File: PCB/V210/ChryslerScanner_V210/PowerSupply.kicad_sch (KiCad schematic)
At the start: 32 parts, among them J4 PROG EN, U5 SDB628, U6 TD1509, U7 TD1509P5, U8 AMS1117-3.3, U9 LM317_SOT-223

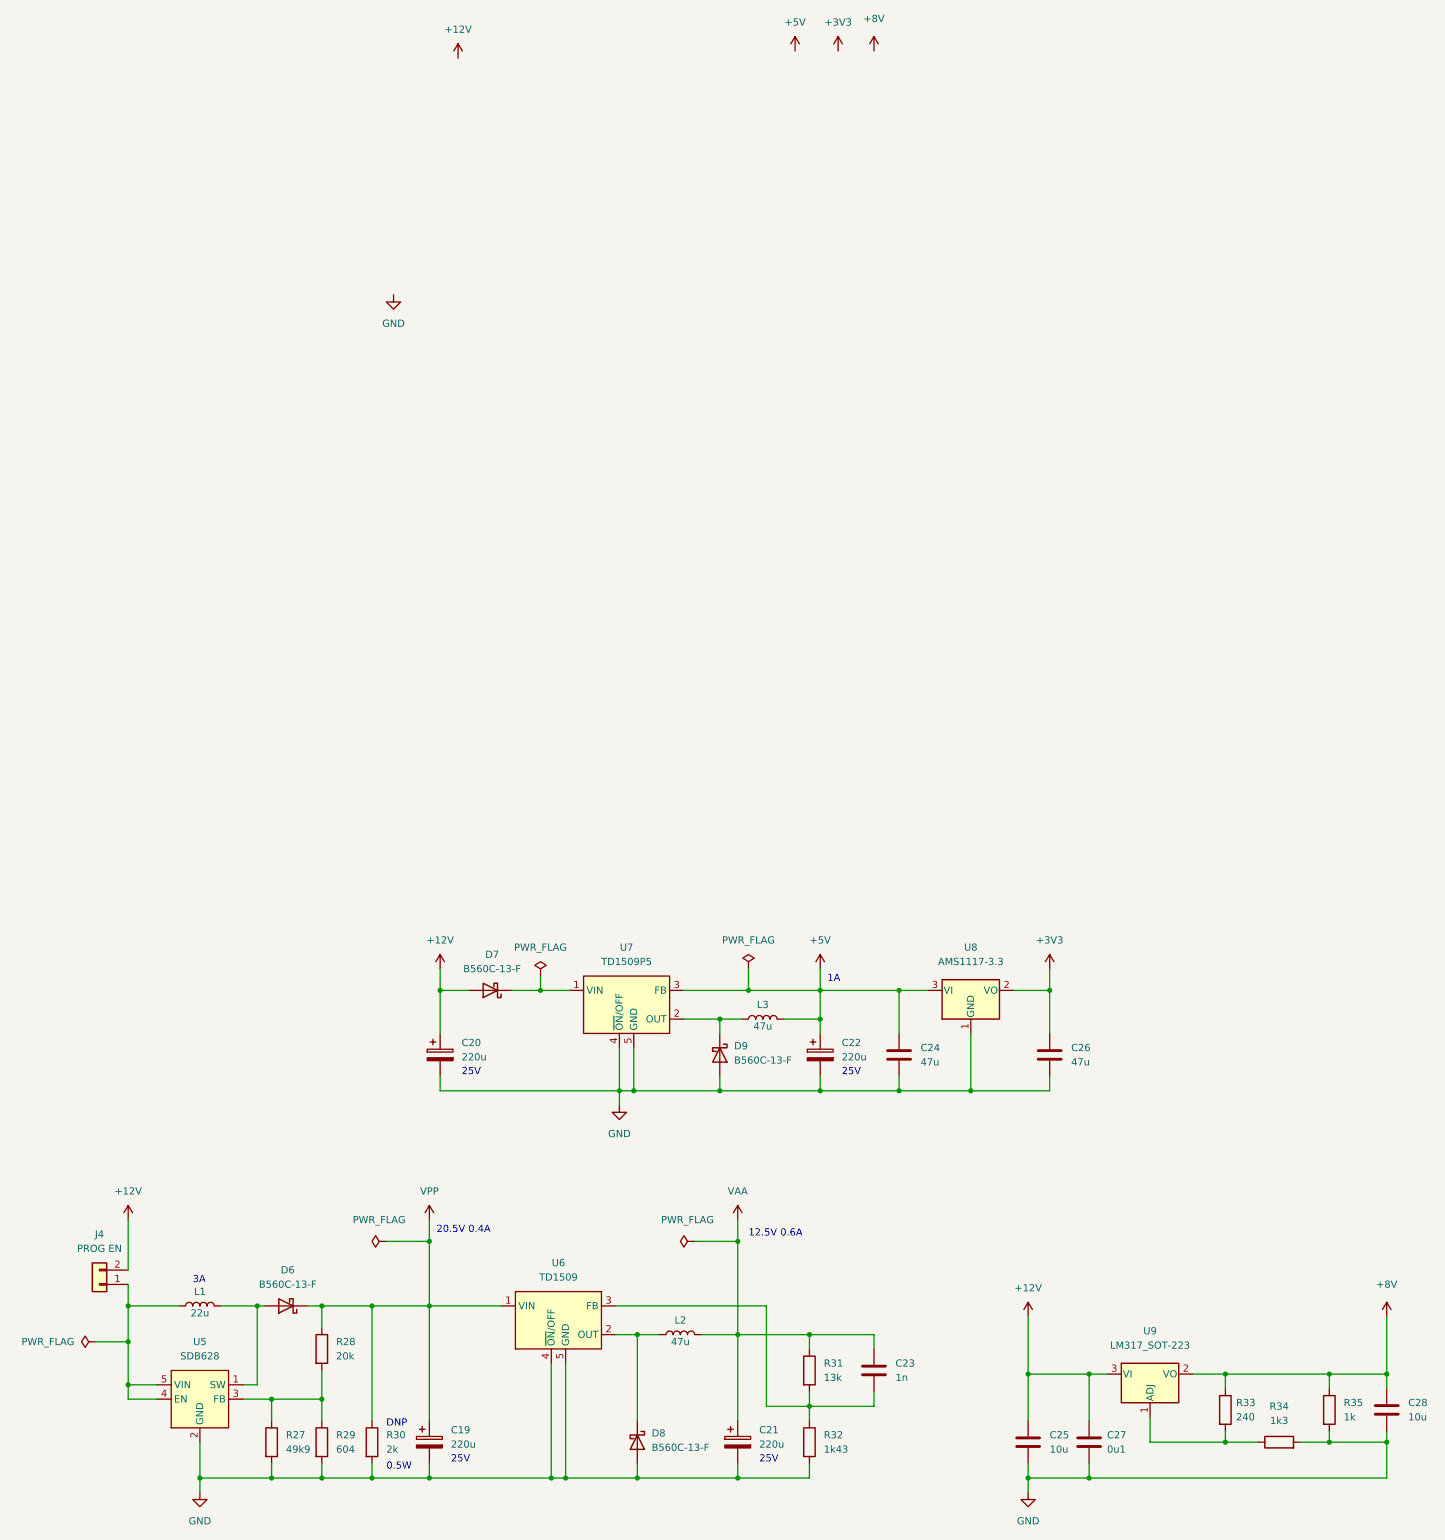
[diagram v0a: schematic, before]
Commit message: Working on power supplies. Added datasheets.
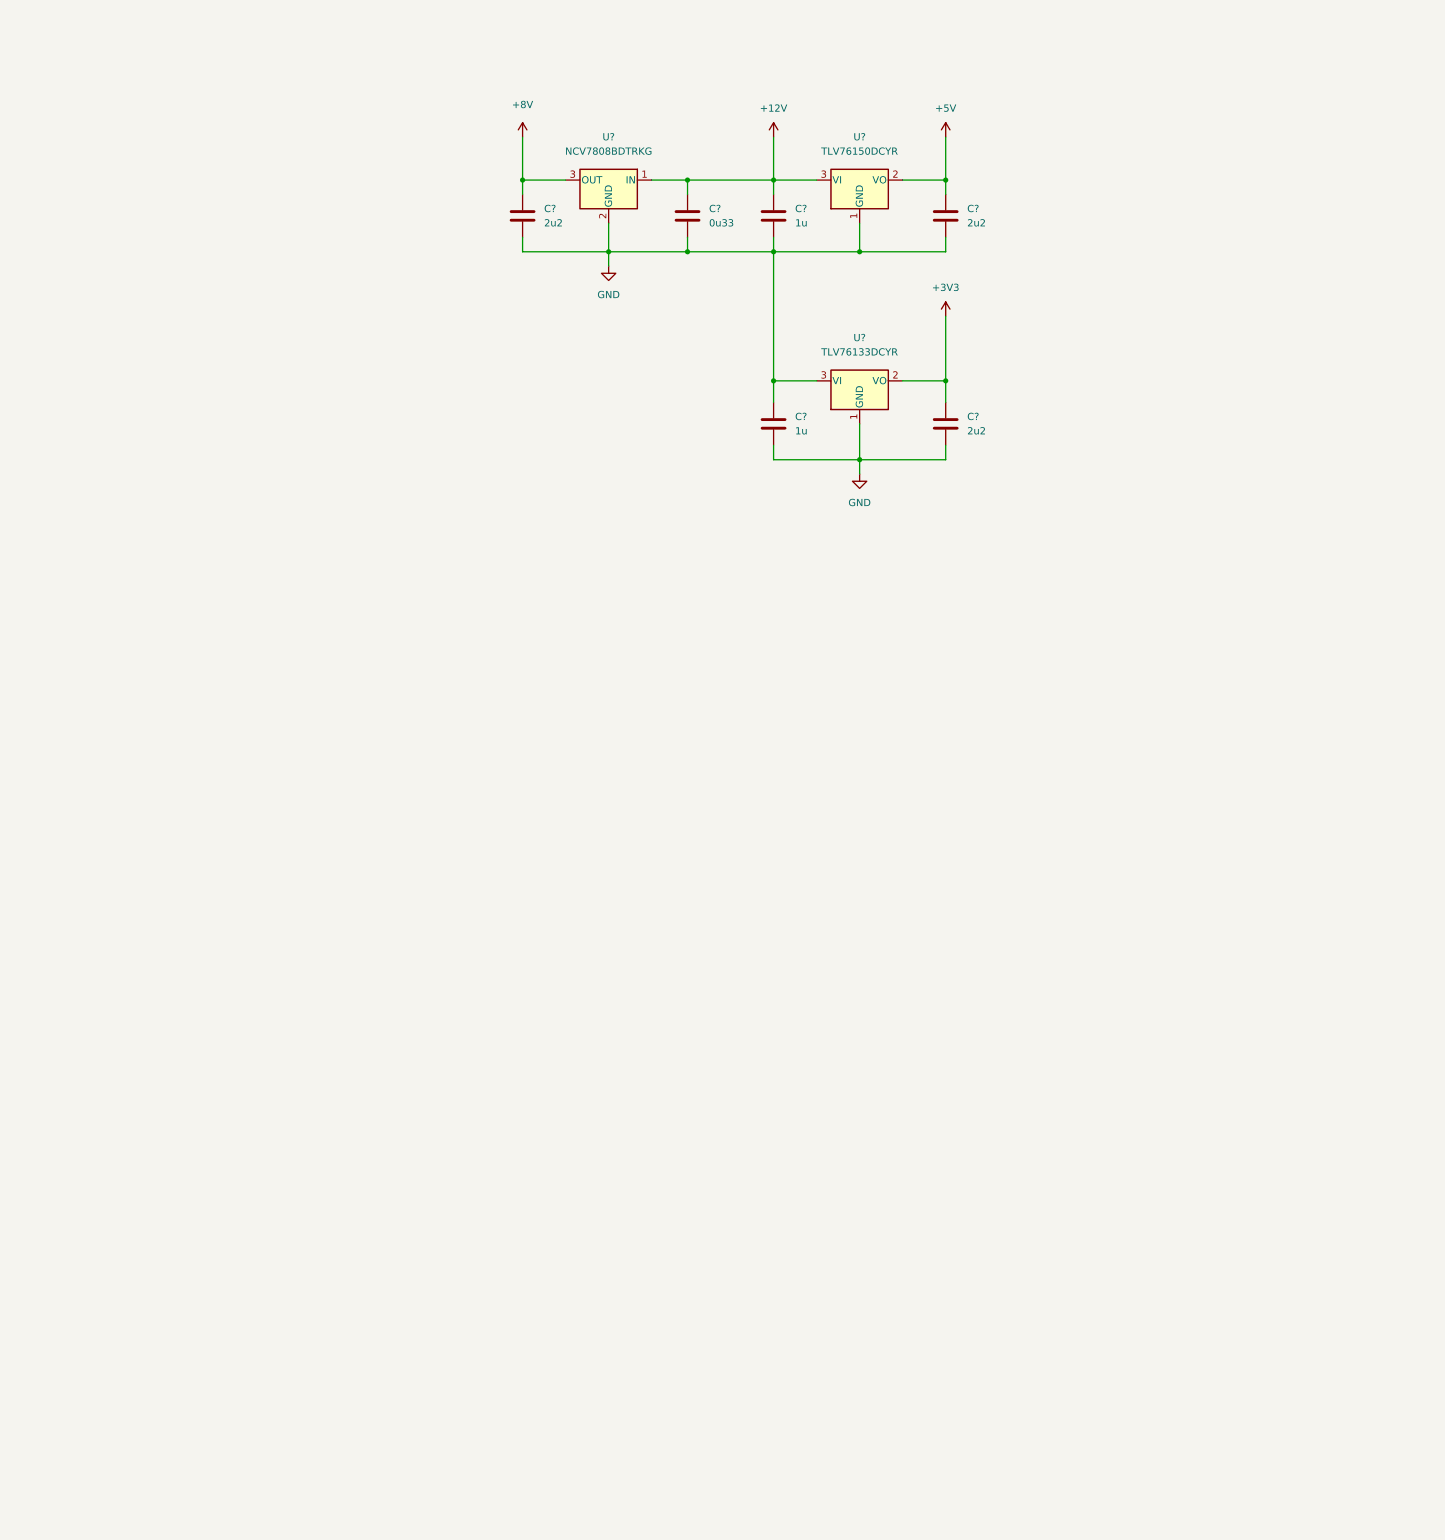
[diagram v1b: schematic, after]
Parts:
- removed C19, C20, C21, C22: 220u, symbol Device:C_Polarized
- removed C23: 1n, Capacitor_SMD:C_0603_1608Metric, symbol Device:C
- removed C24, C26: 47u, symbol Device:C
- removed C25, C28: 10u, Capacitor_SMD:C_0603_1608Metric, symbol Device:C
- removed C27: 0u1, Capacitor_SMD:C_0603_1608Metric, symbol Device:C
- removed D6, D7, D8, D9: B560C-13-F, Diode_SMD:D_SMC, symbol Device:D_Schottky
- removed J4: PROG EN, Connector_PinHeader_2.54mm:PinHeader_1x02_P2.54mm_Vertical, symbol Connector_Generic:Conn_01x02
- removed L1: 22u, symbol Device:L
- removed L2, L3: 47u, symbol Device:L
- removed R27: 49k9, Resistor_SMD:R_0603_1608Metric, symbol Device:R
- removed R28: 20k, Resistor_SMD:R_0603_1608Metric, symbol Device:R
- removed R29: 604, Resistor_SMD:R_0603_1608Metric, symbol Device:R
- removed R30: 2k, Resistor_SMD:R_0603_1608Metric, symbol Device:R
- removed R31: 13k, Resistor_SMD:R_0603_1608Metric, symbol Device:R
- removed R32: 1k43, Resistor_SMD:R_0603_1608Metric, symbol Device:R
- removed R33: 240, Resistor_SMD:R_0603_1608Metric, symbol Device:R
- removed R34: 1k3, Resistor_SMD:R_0603_1608Metric, symbol Device:R
- removed R35: 1k, Resistor_SMD:R_0603_1608Metric, symbol Device:R
- removed U5: SDB628, symbol ChryslerScanner:SD8628
- removed U6: TD1509, symbol ChryslerScanner:TD1509
- removed U7: TD1509P5, symbol ChryslerScanner:TD1509
- removed U8: AMS1117-3.3, symbol Regulator_Linear:AMS1117-3.3
- removed U9: LM317_SOT-223, symbol Regulator_Linear:LM317_SOT-223
- added C?: 0u33, symbol Device:C
- added C? (x3): 2u2, symbol Device:C
- added C? (x2): 1u, symbol Device:C
- added U?: NCV7808BDTRKG, Package_TO_SOT_SMD:TO-252-2, symbol ChryslerScanner:NCV7808BDTRKG
- added U?: TLV76133DCYR, Package_TO_SOT_SMD:SOT-223-3_TabPin2, symbol Regulator_Linear:LM1117-3.3
- added U?: TLV76150DCYR, Package_TO_SOT_SMD:SOT-223-3_TabPin2, symbol Regulator_Linear:LM1117-5.0
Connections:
- net +12V: now also C?.1, C?.1, U?.1 (IN), U?.3 (VI)
- net +3V3: now also C?.1, U?.2 (VO)
- net +5V: now also C?.1, U?.2 (VO)
- net +8V: now also C?.1, U?.3 (OUT)
- net GND: now also C?.1, C?.2, C?.2, C?.2, C?.2, C?.2, C?.2, U?.1 (GND), U?.1 (GND), U?.2 (GND), U?.3 (VI)
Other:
- note removed: "0.5W"
- note removed: "12.5V 0.6A"
- note removed: "1A"
- note removed: "20.5V 0.4A"
- note removed: "25V"
- note removed: "3A"
- note removed: "DNP"

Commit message: Added OBD-II connector.
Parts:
- gave numbers to parts that had none: 9
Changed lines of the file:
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@@
   (title_block
     (title "TJ Diag")
-    (date "2023-07-01")
+    (date "2023-07-06")
     (rev "V1.00")
     (company "andy@britishideas.com")
     (comment 1 "V210/ChryslerScanner_V210/schematic/ChryslerScanner_V210_schematic.pdf")
-    (comment 2 "Developed From: https://github.com/laszlodaniel/ChryslerScanner/blob/master/PCB/")
+    (comment 2 "Based on: https://github.com/laszlodaniel/ChryslerScanner/blob/master/PCB/")
     (comment 3 "GPL V3 LICENSE")
   )
@@
   (symbol (lib_id "Device:C") (at 137.16 85.09 0) (unit 1)
     (in_bom yes) (on_board yes) (fields_autoplaced)
-    (property "Reference" "C?" (id 0) (at 140.97 83.8199 0)
+    (property "Reference" "C20" (id 0) (at 140.97 83.8199 0)
       (effects (font (size 1.27 1.27)) (justify left))
     )
@@
   (symbol (lib_id "power:+3V3") (at 182.88 102.87 0) (unit 1)
     (in_bom yes) (on_board yes) (fields_autoplaced)
-    (property "Reference" "#PWR051" (id 0) (at 182.88 106.68 0)
+    (property "Reference" "#PWR046" (id 0) (at 182.88 106.68 0)
       (effects (font (size 1.27 1.27)) hide)
     )
@@
   (symbol (lib_id "ChryslerScanner:NCV7808BDTRKG") (at 123.19 78.74 0) (mirror y) (unit 1)
     (in_bom yes) (on_board yes) (fields_autoplaced)
-    (property "Reference" "U?" (id 0) (at 123.19 71.12 0))
+    (property "Reference" "U5" (id 0) (at 123.19 71.12 0))
     (property "Value" "NCV7808BDTRKG" (id 1) (at 123.19 73.66 0))
     (property "Footprint" "Package_TO_SOT_SMD:TO-252-2" (id 2) (at 123.19 73.66 0)
@@
   (symbol (lib_id "Device:C") (at 182.88 121.92 0) (unit 1)
     (in_bom yes) (on_board yes) (fields_autoplaced)
-    (property "Reference" "C?" (id 0) (at 186.69 120.6499 0)
+    (property "Reference" "C24" (id 0) (at 186.69 120.6499 0)
       (effects (font (size 1.27 1.27)) (justify left))
     )
@@
   (symbol (lib_id "Device:C") (at 107.95 85.09 0) (unit 1)
     (in_bom yes) (on_board yes) (fields_autoplaced)
-    (property "Reference" "C?" (id 0) (at 111.76 83.8199 0)
+    (property "Reference" "C19" (id 0) (at 111.76 83.8199 0)
       (effects (font (size 1.27 1.27)) (justify left))
     )
@@
   (symbol (lib_id "power:GND") (at 123.19 93.98 0) (unit 1)
     (in_bom yes) (on_board yes) (fields_autoplaced)
-    (property "Reference" "#PWR043" (id 0) (at 123.19 100.33 0)
+    (property "Reference" "#PWR042" (id 0) (at 123.19 100.33 0)
       (effects (font (size 1.27 1.27)) hide)
     )
@@
   (symbol (lib_id "power:+5V") (at 182.88 71.12 0) (unit 1)
     (in_bom yes) (on_board yes) (fields_autoplaced)
-    (property "Reference" "#PWR049" (id 0) (at 182.88 74.93 0)
+    (property "Reference" "#PWR045" (id 0) (at 182.88 74.93 0)
       (effects (font (size 1.27 1.27)) hide)
     )
@@
   (symbol (lib_id "Regulator_Linear:LM1117-3.3") (at 167.64 114.3 0) (unit 1)
     (in_bom yes) (on_board yes) (fields_autoplaced)
-    (property "Reference" "U?" (id 0) (at 167.64 106.68 0))
+    (property "Reference" "U7" (id 0) (at 167.64 106.68 0))
     (property "Value" "TLV76133DCYR" (id 1) (at 167.64 109.22 0))
     (property "Footprint" "Package_TO_SOT_SMD:SOT-223-3_TabPin2" (id 2) (at 167.64 114.3 0)
@@
   (symbol (lib_id "power:GND") (at 167.64 130.81 0) (unit 1)
     (in_bom yes) (on_board yes) (fields_autoplaced)
-    (property "Reference" "#PWR?" (id 0) (at 167.64 137.16 0)
+    (property "Reference" "#PWR044" (id 0) (at 167.64 137.16 0)
       (effects (font (size 1.27 1.27)) hide)
     )
@@
   (symbol (lib_id "Device:C") (at 182.88 85.09 0) (unit 1)
     (in_bom yes) (on_board yes) (fields_autoplaced)
-    (property "Reference" "C?" (id 0) (at 186.69 83.8199 0)
+    (property "Reference" "C23" (id 0) (at 186.69 83.8199 0)
       (effects (font (size 1.27 1.27)) (justify left))
     )
@@
   (symbol (lib_id "power:+8V") (at 107.95 71.12 0) (unit 1)
     (in_bom yes) (on_board yes) (fields_autoplaced)
-    (property "Reference" "#PWR052" (id 0) (at 107.95 74.93 0)
+    (property "Reference" "#PWR041" (id 0) (at 107.95 74.93 0)
       (effects (font (size 1.27 1.27)) hide)
     )
@@
   (symbol (lib_id "Device:C") (at 152.4 121.92 0) (unit 1)
     (in_bom yes) (on_board yes) (fields_autoplaced)
-    (property "Reference" "C?" (id 0) (at 156.21 120.6499 0)
+    (property "Reference" "C22" (id 0) (at 156.21 120.6499 0)
       (effects (font (size 1.27 1.27)) (justify left))
     )
@@
   (symbol (lib_id "Regulator_Linear:LM1117-5.0") (at 167.64 78.74 0) (unit 1)
     (in_bom yes) (on_board yes) (fields_autoplaced)
-    (property "Reference" "U?" (id 0) (at 167.64 71.12 0))
+    (property "Reference" "U6" (id 0) (at 167.64 71.12 0))
     (property "Value" "TLV76150DCYR" (id 1) (at 167.64 73.66 0))
     (property "Footprint" "Package_TO_SOT_SMD:SOT-223-3_TabPin2" (id 2) (at 167.64 78.74 0)
@@
   (symbol (lib_id "Device:C") (at 152.4 85.09 0) (unit 1)
     (in_bom yes) (on_board yes) (fields_autoplaced)
-    (property "Reference" "C?" (id 0) (at 156.21 83.8199 0)
+    (property "Reference" "C21" (id 0) (at 156.21 83.8199 0)
       (effects (font (size 1.27 1.27)) (justify left))
     )
@@
   (symbol (lib_id "power:+12V") (at 152.4 71.12 0) (unit 1)
     (in_bom yes) (on_board yes) (fields_autoplaced)
-    (property "Reference" "#PWR046" (id 0) (at 152.4 74.93 0)
-      (effects (font (size 1.27 1.27)) hide)
-    )
+    (property "Reference" "#PWR043" (id 0) (at 152.4 74.93 0)
+      (effects (font (size 1.27 1.27)) hide)
+    )

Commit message: Added CCD back in - needed for early TJs.
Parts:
- C17: renamed from C19; footprint (none) -> Capacitor_SMD:C_0603_1608Metric
- C18: renamed from C20; footprint (none) -> Capacitor_SMD:C_0603_1608Metric
- C19: renamed from C21; footprint (none) -> Capacitor_SMD:C_0603_1608Metric
- C20: renamed from C22; footprint (none) -> Capacitor_SMD:C_0603_1608Metric
- C21: renamed from C23; footprint (none) -> Capacitor_SMD:C_0603_1608Metric
- C22: renamed from C24; footprint (none) -> Capacitor_SMD:C_0603_1608Metric
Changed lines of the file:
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@@
   (title_block
     (title "TJ Diag")
-    (date "2023-07-06")
+    (date "2023-07-07")
     (rev "V1.00")
     (company "andy@britishideas.com")
@@
   (symbol (lib_id "Device:C") (at 137.16 85.09 0) (unit 1)
     (in_bom yes) (on_board yes) (fields_autoplaced)
-    (property "Reference" "C20" (id 0) (at 140.97 83.8199 0)
+    (property "Reference" "C18" (id 0) (at 140.97 83.8199 0)
       (effects (font (size 1.27 1.27)) (justify left))
     )
@@
       (effects (font (size 1.27 1.27)) (justify left))
     )
-    (property "Footprint" "" (id 2) (at 138.1252 88.9 0)
+    (property "Footprint" "Capacitor_SMD:C_0603_1608Metric" (id 2) (at 138.1252 88.9 0)
       (effects (font (size 1.27 1.27)) hide)
     )
@@
   (symbol (lib_id "power:+3V3") (at 182.88 102.87 0) (unit 1)
     (in_bom yes) (on_board yes) (fields_autoplaced)
-    (property "Reference" "#PWR046" (id 0) (at 182.88 106.68 0)
+    (property "Reference" "#PWR042" (id 0) (at 182.88 106.68 0)
       (effects (font (size 1.27 1.27)) hide)
     )
@@
   (symbol (lib_id "Device:C") (at 182.88 121.92 0) (unit 1)
     (in_bom yes) (on_board yes) (fields_autoplaced)
-    (property "Reference" "C24" (id 0) (at 186.69 120.6499 0)
+    (property "Reference" "C22" (id 0) (at 186.69 120.6499 0)
       (effects (font (size 1.27 1.27)) (justify left))
     )
@@
       (effects (font (size 1.27 1.27)) (justify left))
     )
-    (property "Footprint" "" (id 2) (at 183.8452 125.73 0)
+    (property "Footprint" "Capacitor_SMD:C_0603_1608Metric" (id 2) (at 183.8452 125.73 0)
       (effects (font (size 1.27 1.27)) hide)
     )
@@
   (symbol (lib_id "Device:C") (at 107.95 85.09 0) (unit 1)
     (in_bom yes) (on_board yes) (fields_autoplaced)
-    (property "Reference" "C19" (id 0) (at 111.76 83.8199 0)
+    (property "Reference" "C17" (id 0) (at 111.76 83.8199 0)
       (effects (font (size 1.27 1.27)) (justify left))
     )
@@
       (effects (font (size 1.27 1.27)) (justify left))
     )
-    (property "Footprint" "" (id 2) (at 108.9152 88.9 0)
+    (property "Footprint" "Capacitor_SMD:C_0603_1608Metric" (id 2) (at 108.9152 88.9 0)
       (effects (font (size 1.27 1.27)) hide)
     )
@@
   (symbol (lib_id "power:GND") (at 123.19 93.98 0) (unit 1)
     (in_bom yes) (on_board yes) (fields_autoplaced)
-    (property "Reference" "#PWR042" (id 0) (at 123.19 100.33 0)
+    (property "Reference" "#PWR038" (id 0) (at 123.19 100.33 0)
       (effects (font (size 1.27 1.27)) hide)
     )
@@
   (symbol (lib_id "power:+5V") (at 182.88 71.12 0) (unit 1)
     (in_bom yes) (on_board yes) (fields_autoplaced)
-    (property "Reference" "#PWR045" (id 0) (at 182.88 74.93 0)
+    (property "Reference" "#PWR041" (id 0) (at 182.88 74.93 0)
       (effects (font (size 1.27 1.27)) hide)
     )
@@
   (symbol (lib_id "power:GND") (at 167.64 130.81 0) (unit 1)
     (in_bom yes) (on_board yes) (fields_autoplaced)
-    (property "Reference" "#PWR044" (id 0) (at 167.64 137.16 0)
+    (property "Reference" "#PWR040" (id 0) (at 167.64 137.16 0)
       (effects (font (size 1.27 1.27)) hide)
     )
@@
   (symbol (lib_id "Device:C") (at 182.88 85.09 0) (unit 1)
     (in_bom yes) (on_board yes) (fields_autoplaced)
-    (property "Reference" "C23" (id 0) (at 186.69 83.8199 0)
+    (property "Reference" "C21" (id 0) (at 186.69 83.8199 0)
       (effects (font (size 1.27 1.27)) (justify left))
     )
@@
       (effects (font (size 1.27 1.27)) (justify left))
     )
-    (property "Footprint" "" (id 2) (at 183.8452 88.9 0)
+    (property "Footprint" "Capacitor_SMD:C_0603_1608Metric" (id 2) (at 183.8452 88.9 0)
       (effects (font (size 1.27 1.27)) hide)
     )
@@
   (symbol (lib_id "power:+8V") (at 107.95 71.12 0) (unit 1)
     (in_bom yes) (on_board yes) (fields_autoplaced)
-    (property "Reference" "#PWR041" (id 0) (at 107.95 74.93 0)
+    (property "Reference" "#PWR037" (id 0) (at 107.95 74.93 0)
       (effects (font (size 1.27 1.27)) hide)
     )
@@
   (symbol (lib_id "Device:C") (at 152.4 121.92 0) (unit 1)
     (in_bom yes) (on_board yes) (fields_autoplaced)
-    (property "Reference" "C22" (id 0) (at 156.21 120.6499 0)
+    (property "Reference" "C20" (id 0) (at 156.21 120.6499 0)
       (effects (font (size 1.27 1.27)) (justify left))
     )
@@
       (effects (font (size 1.27 1.27)) (justify left))
     )
-    (property "Footprint" "" (id 2) (at 153.3652 125.73 0)
+    (property "Footprint" "Capacitor_SMD:C_0603_1608Metric" (id 2) (at 153.3652 125.73 0)
       (effects (font (size 1.27 1.27)) hide)
     )
@@
   (symbol (lib_id "Device:C") (at 152.4 85.09 0) (unit 1)
     (in_bom yes) (on_board yes) (fields_autoplaced)
-    (property "Reference" "C21" (id 0) (at 156.21 83.8199 0)
+    (property "Reference" "C19" (id 0) (at 156.21 83.8199 0)
       (effects (font (size 1.27 1.27)) (justify left))
     )
@@
       (effects (font (size 1.27 1.27)) (justify left))
     )
-    (property "Footprint" "" (id 2) (at 153.3652 88.9 0)
+    (property "Footprint" "Capacitor_SMD:C_0603_1608Metric" (id 2) (at 153.3652 88.9 0)
       (effects (font (size 1.27 1.27)) hide)
     )
@@
   (symbol (lib_id "power:+12V") (at 152.4 71.12 0) (unit 1)
     (in_bom yes) (on_board yes) (fields_autoplaced)
-    (property "Reference" "#PWR043" (id 0) (at 152.4 74.93 0)
-      (effects (font (size 1.27 1.27)) hide)
-    )
+    (property "Reference" "#PWR039" (id 0) (at 152.4 74.93 0)
+      (effects (font (size 1.27 1.27)) hide)
+    )
